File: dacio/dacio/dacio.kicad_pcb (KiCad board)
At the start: 4 copper layers, 90.2 x 53.1 mm, 49 parts, among them J3 RJ45_Shielded, J4 RJ45_Shielded, J5 Conn_01x16_Socket, U1 SN74LVC1T45DBV, U10 MAX3232, U11 MAX3232, U12 74HCT32D, U13 74HCT00D, U14 74HCT32D, U15 74HCT00D, U16 SN74LVC1T45DBV, U18 SN74LVC1T45DBV, U2 SN74LVC1T45DBV, U3 TLV70018_SOT353, U4 MAX487CSA+, U5 MAX487CSA+, U6 MAX487CSA+, U7 MAX487CSA+, U8 MAX487CSA+, U9 MAX487CSA+

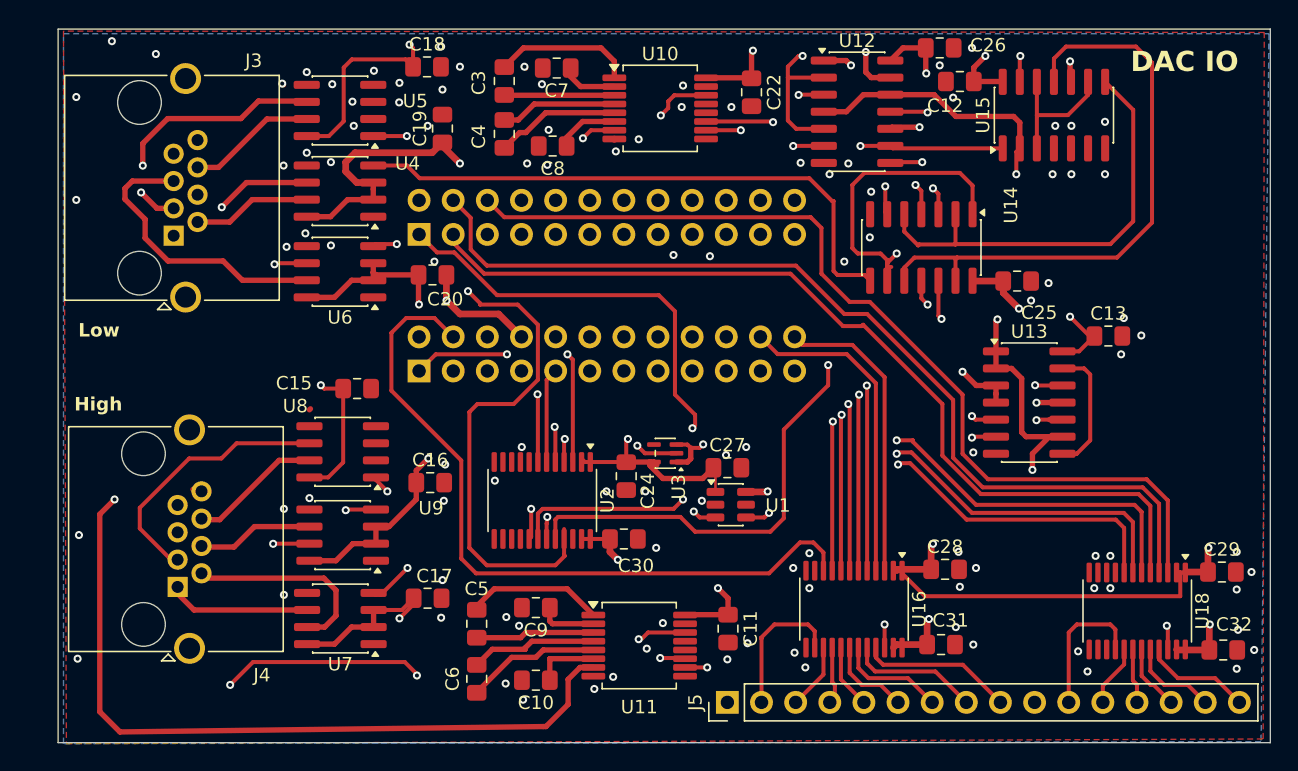
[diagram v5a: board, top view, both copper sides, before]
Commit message: Updated footprints for RJ45 and balun height.
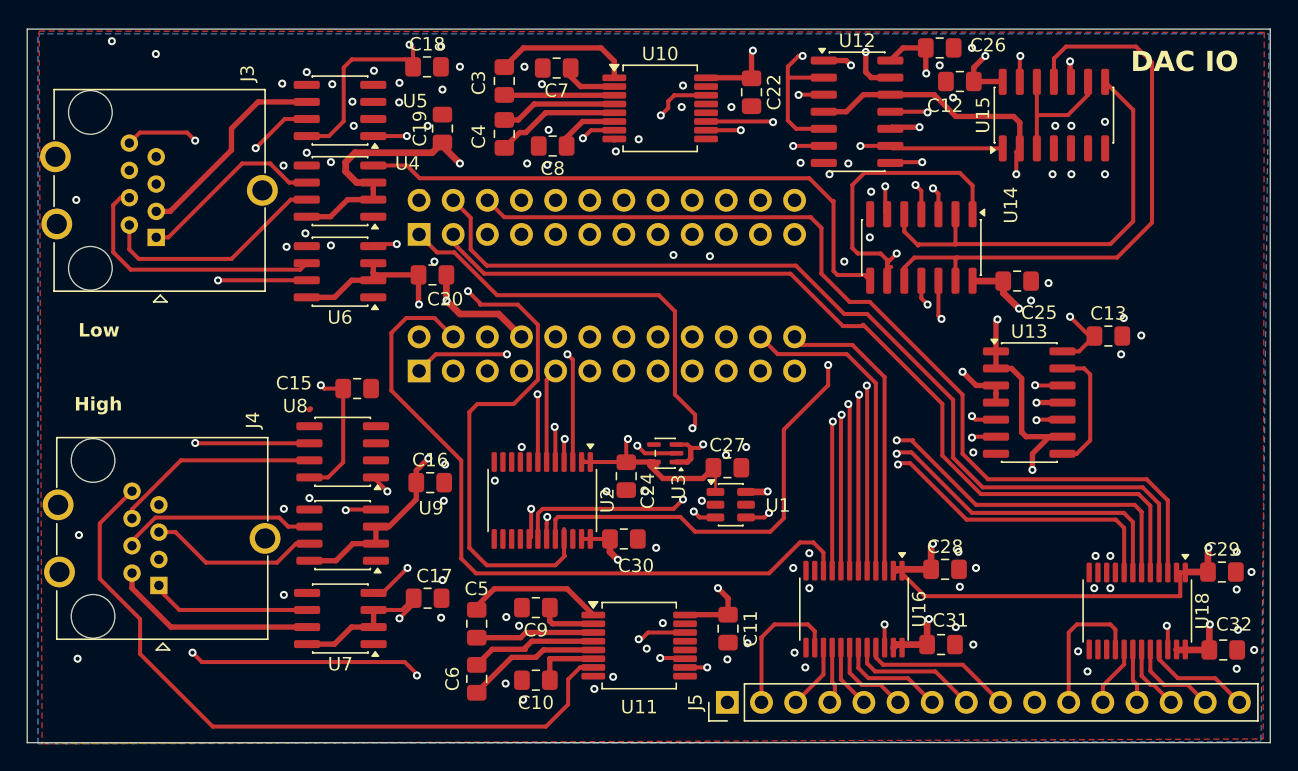
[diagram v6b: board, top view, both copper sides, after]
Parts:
- J3, J4: footprint Connector_RJ:RJ45_Amphenol_RJHSE5380 -> custom:RJ45
- moved J4 7.50 mm to (142.2, 113.1), turned to -90 degrees
- moved J3 7.24 mm to (142.0, 87.2), turned to -90 degrees
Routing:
- net Net-(U9-B): track 34.9 -> 12.7 mm, vias 1 -> 0
- net Net-(U11-T2OUT): track 65.4 -> 53.2 mm, vias 1 -> 0
- net Net-(U4-B): track 8.81 -> 17.1 mm
- net Net-(U6-A): track 12.4 -> 20.1 mm, vias 1 -> 0
- net Net-(U10-T2OUT): track 31.9 -> 38.2 mm, vias 1 -> 2
- net Net-(U9-A): track 9.07 -> 14.6 mm
- net Net-(U5-B): track 9.62 -> 14.8 mm, vias 0 -> 1
- net Net-(U8-B): track 10.3 -> 15.4 mm
- net Net-(U11-T1OUT): track 61.2 -> 56.3 mm
- net Net-(U5-A): track 20.1 -> 15.6 mm, vias 2 -> 0
- net Net-(U6-B): track 21.5 -> 17.1 mm, vias 0 -> 1
- net Net-(U4-A): track 12.8 -> 14.1 mm, vias 1 -> 0
- net Net-(U7-A): track 10.7 -> 12.0 mm
- net Net-(U8-A): track 19.3 -> 18.3 mm, vias 0 -> 1
- net Net-(U10-T1OUT): track 42.7 -> 43.3 mm
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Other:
- board size 90.2 x 53.1 mm -> 92.5 x 53.1 mm

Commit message: Finalized the PCBs and sent them to review.
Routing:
- net GND: track 16.7 -> 16.6 mm, vias 105 -> 171
